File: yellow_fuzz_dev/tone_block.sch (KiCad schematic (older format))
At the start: 34 parts

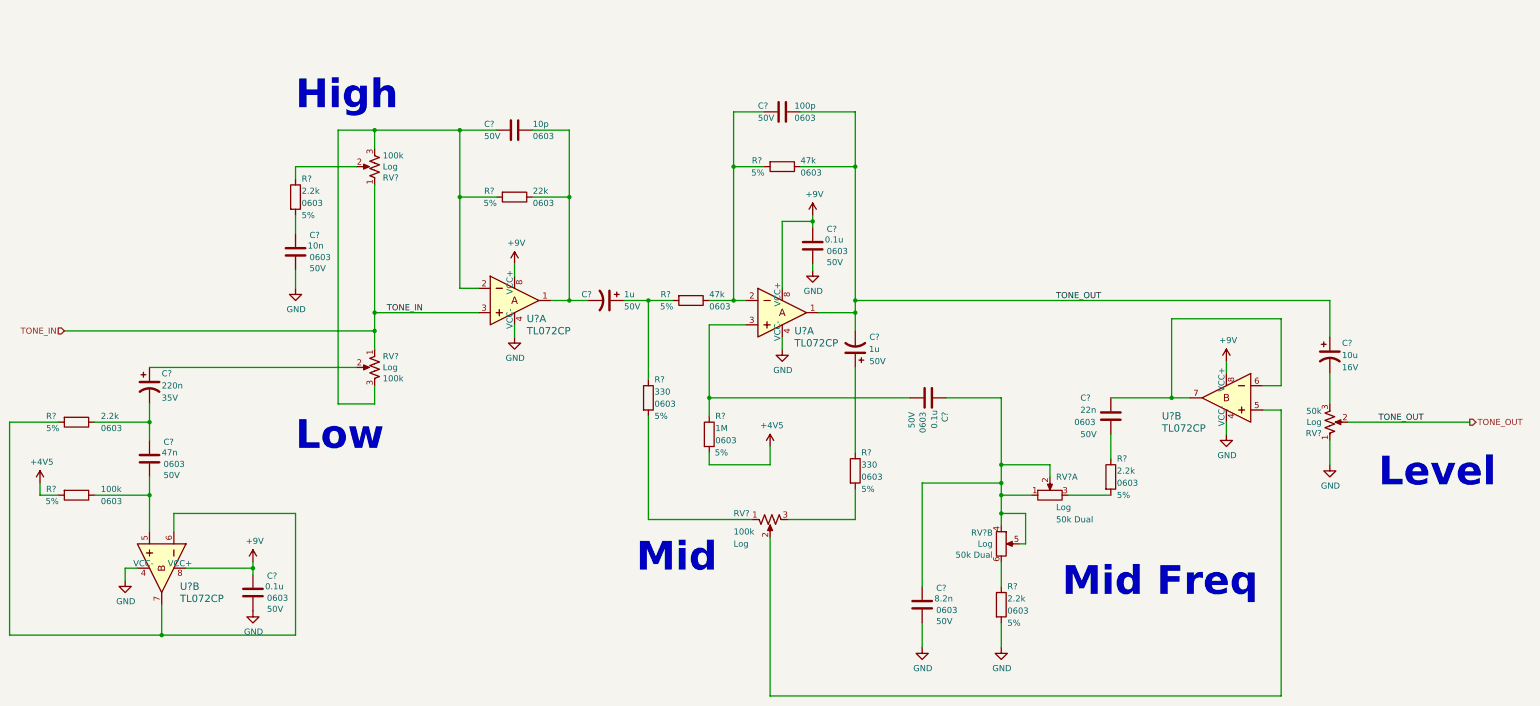
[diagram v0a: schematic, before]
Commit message: moved footprints into PCB
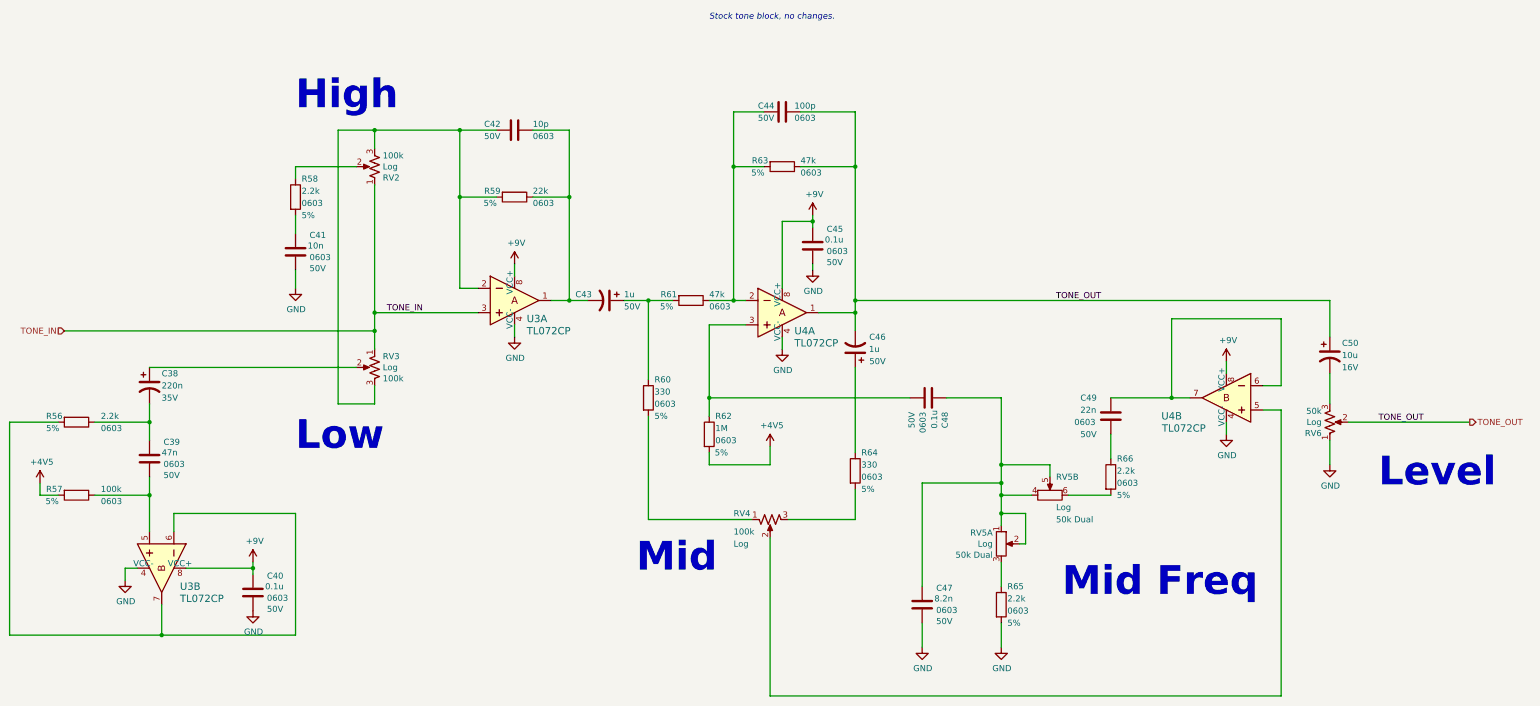
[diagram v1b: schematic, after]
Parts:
- C38, C50: renamed from C?; footprint (none) -> Capacitor_THT:CP_Radial_D5.0mm_P2.00mm
- C43, C46: renamed from C?; footprint (none) -> Capacitor_THT:CP_Radial_D4.0mm_P1.50mm
- U3, U4: renamed from U?; footprint digikey-footprints:DIP-8_W7.62mm -> digikey:DIP-8_W7.62mm
- gave numbers to parts that had none: 25
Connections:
- net at R65.1: now also RV5.3; no longer RV5.6
- net at R66.2: now also RV5.6; no longer RV5.3
- new net: C47.1, C48.1, RV5.1, RV5.2, RV5.4, RV5.5
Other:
- note added: "Stock tone block, no changes."

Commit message: added 3d to connector and DIP footprints, moved to project lib, updated PCB
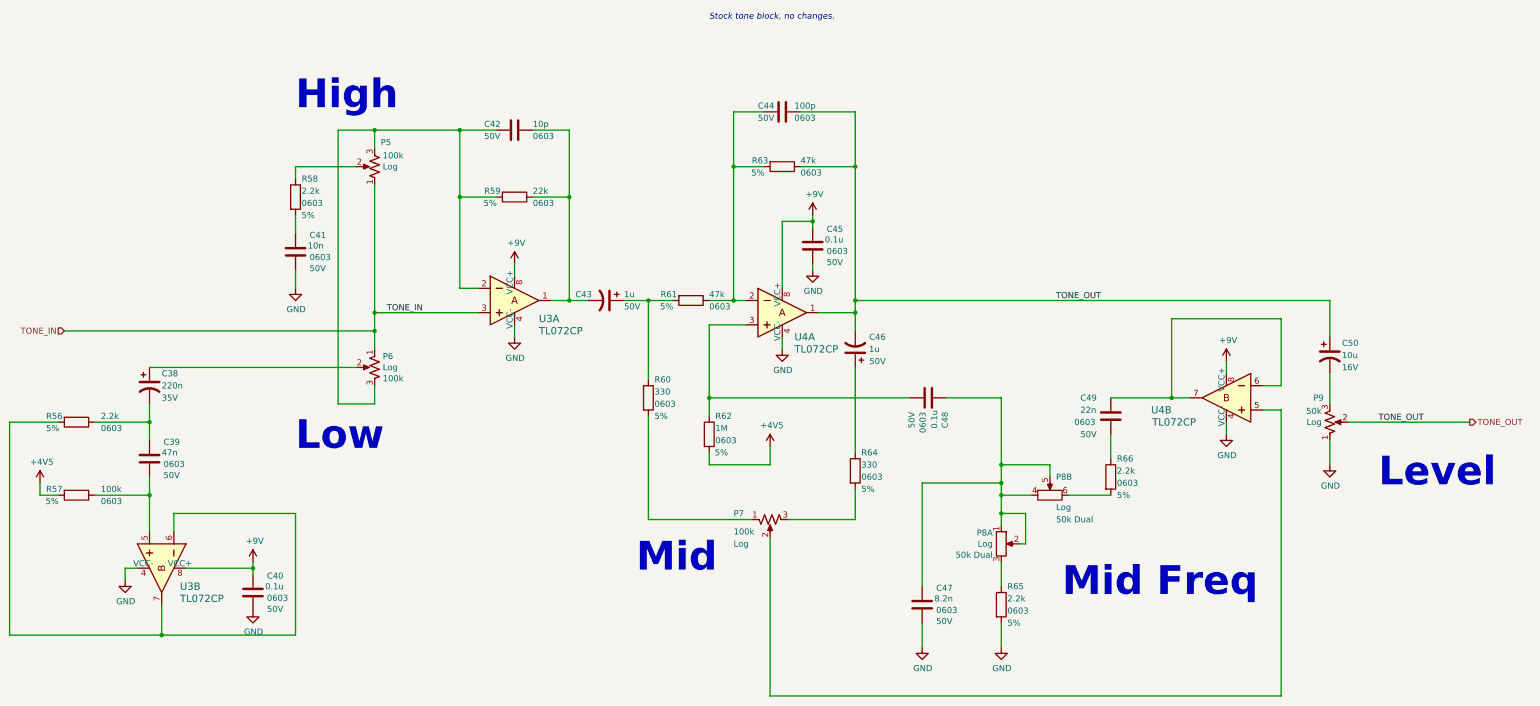
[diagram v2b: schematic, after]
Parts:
- removed U3, U4: TL072CP, digikey:DIP-8_W7.62mm, symbol dk_opamps:TL072CP
- added U3, U4: TL072CP, yellow_fuzz_dev:DIP-8_W7.62mm, symbol yellow_fuzz_dev:TL072CP
- renumbered RV2 to P5, RV3 to P6, RV4 to P7, RV5 to P8, RV6 to P9
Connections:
- net +9V: now also U3.8 (VCC+), U3.8 (VCC+), U4.8 (VCC+), U4.8 (VCC+)
- net GND: now also U3.4 (VCC-), U3.4 (VCC-), U4.4 (VCC-), U4.4 (VCC-)
- net TONE_IN: now also U3.3
- net TONE_OUT: now also U4.1
- net at C42.1, C43.2, R59.1: now also U3.1
- net at C42.2, P5.3, P6.3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: now also U3.2
- net at C44.2, R61.1, R63.2: now also U4.2
- net at R56.2: now also U3.6, U3.7
- net at C39.2, R57.1: now also U3.5
- net at C48.2, R62.1: now also U4.3
- net at P7.2: now also U4.5
- net at C49.1: now also U4.6, U4.7

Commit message: updated potentiometers to use the same mechanical family throughout
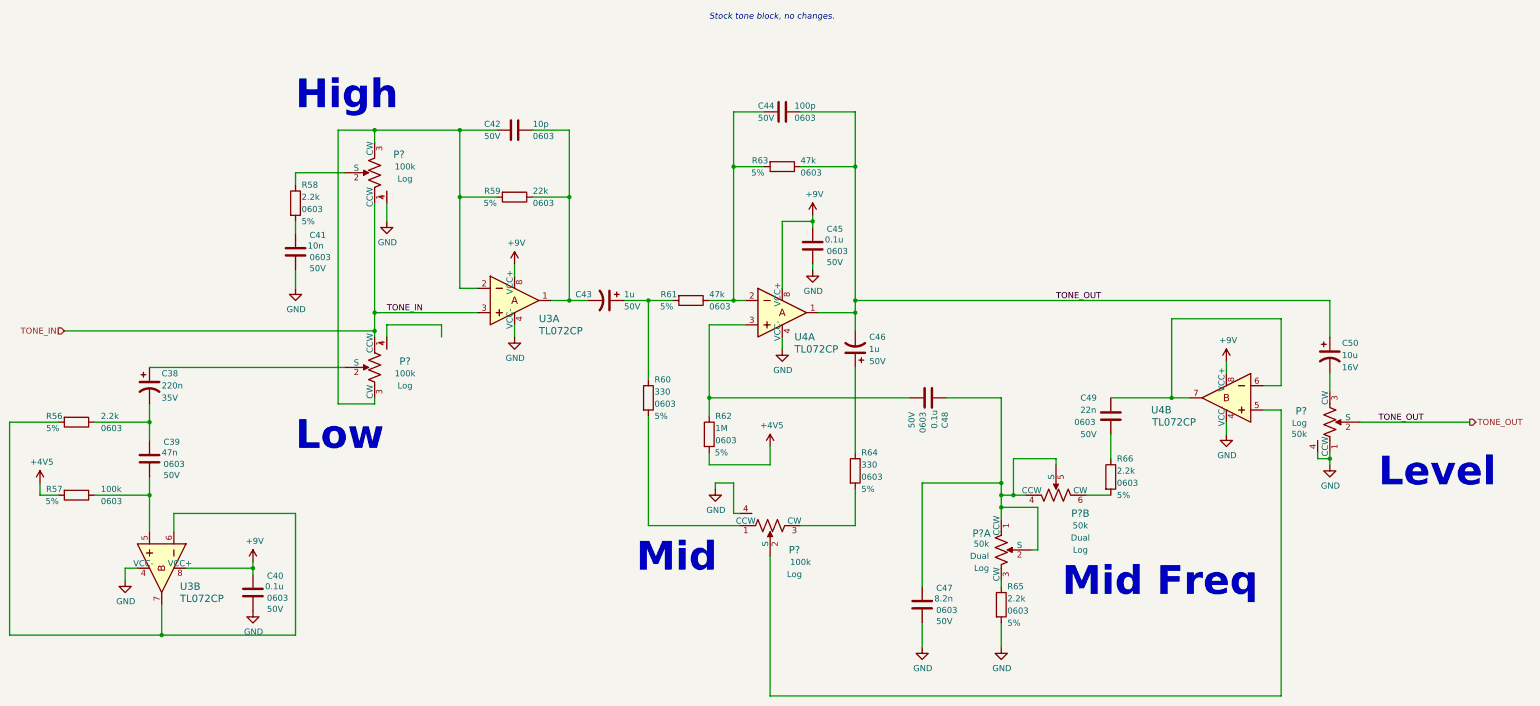
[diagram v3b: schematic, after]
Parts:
- removed P5, P6, P7: R_POT_US, yellow_fuzz_dev:Potentiometer_Bourns_PTV111_4420A_Single_Vertical, symbol Device:R_POT_US
- removed P8: R_POT_Dual_Separate, yellow_fuzz_dev:Potentiometer_Bourns_PTV112_3417A_Dual_Vertical, symbol Device:R_POT_Dual_Separate
- removed P9: R_POT_US, yellow_fuzz_dev:Potentiometer_Bourns_PCW1J_R24_B_Single_Vertical, symbol Device:R_POT_US
- added P? (x2): PTV112-4420A-A503, yellow_fuzz_dev:Potentiometer_Bourns_PTV112_3417A_Dual_Vertical, symbol yellow_fuzz_dev:PTV112-4420A-A503
- added P?: PTV111-4420A-A503, yellow_fuzz_dev:Potentiometer_Bourns_PTV111_4420A_Single_Vertical, symbol yellow_fuzz_dev:PTV111-4420A-A503
- added P? (x3): PTV111-4420A-A104, yellow_fuzz_dev:Potentiometer_Bourns_PTV111_4420A_Single_Vertical, symbol yellow_fuzz_dev:PTV111-4420A-A104
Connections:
- net GND: now also P?.1 (CCW), P?.4, P?.4, P?.4
- net TONE_IN: now also P?.1 (CCW), P?.1 (CCW)
- net TONE_OUT: now also P?.2 (S)
- net at C50.2: now also P?.3 (CW)
- net at C47.1, C48.1: now also P?.1 (CCW), P?.2 (S), P?.4 (CCW), P?.5 (S)
- net at R65.1: now also P?.3 (CW)
- net at C42.2, R59.2, U3.2: now also P?.3 (CW), P?.3 (CW)
- net at R60.2: now also P?.1 (CCW)
- net at R58.1: now also P?.2 (S)
- net at C38.1: now also P?.2 (S)
- net at R64.2: now also P?.3 (CW)
- net at U4.5: now also P?.2 (S)
- net at R66.2: now also P?.6 (CW)
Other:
- moved on the sheet: R58

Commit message: first draft placement done. Added ampharos logo.
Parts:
- gave numbers to parts that had none: 5
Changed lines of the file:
@@
-$EndComp
-$Comp
-L Device:CP1 C46
-U 1 1 5EA96593
-P 9050 4850
-F 0 "C46" H 8800 4750 50  0000 L CNN
-F 1 "1u" H 8850 4850 50  0000 L CNN
-F 2 "Capacitor_THT:CP_Radial_D4.0mm_P1.50mm" H 9050 4850 50  0001 C CNN
-F 3 "~" H 9050 4850 50  0001 C CNN
-F 4 "Nichicon" H 9050 4850 50  0001 C CNN "Manufacturer"
-F 5 "UST1H010MDD1TE" H 9050 4850 50  0001 C CNN "Manufacturer PN"
-F 6 "Digi-Key" H 9050 4850 50  0001 C CNN "Supplier"
-F 7 "493-17436-1-ND" H 9050 4850 50  0001 C CNN "Supplier PN"
-F 8 "50V" H 8800 4950 50  0000 L CNN "Voltage"
-	1    9050 4850
-	-1   0    0    1
-$EndComp
-$Comp
-L Device:R R60
-U 1 1 5EA965A0
-P 7350 5250
-F 0 "R60" H 7400 5400 50  0000 L CNN
-F 1 "330" H 7400 5300 50  0000 L CNN
-F 2 "Resistor_SMD:R_0603_1608Metric_Pad1.05x0.95mm_HandSolder" V 7280 5250 50  0001 C CNN
-F 3 "~" H 7350 5250 50  0001 C CNN
-F 4 "CR0603-JW-331ELF" H 7350 5250 50  0001 C CNN "Manufacturer PN"
-F 5 "5%" H 7400 5100 50  0000 L CNN "Tolerance"
-F 6 "Bourns Inc." H 7350 5250 50  0001 C CNN "Manufacturer"
-F 7 "Digi-Key" H 7350 5250 50  0001 C CNN "Supplier"
-F 8 "CR0603-JW-331ELFCT-ND" H 7350 5250 50  0001 C CNN "Supplier PN"
-F 9 "0.1 W" H 7350 5250 50  0001 C CNN "Power"
-F 10 "0603" H 7400 5200 50  0000 L CNN "Package"
-	1    7350 5250
-	1    0    0    -1
 $EndComp
 $Comp
@@
 $EndComp
 $Comp
-L Device:R R64
-U 1 1 5EA96609
-P 9050 5850
-F 0 "R64" H 9100 6000 50  0000 L CNN
-F 1 "330" H 9100 5900 50  0000 L CNN
-F 2 "Resistor_SMD:R_0603_1608Metric_Pad1.05x0.95mm_HandSolder" V 8980 5850 50  0001 C CNN
-F 3 "~" H 9050 5850 50  0001 C CNN
-F 4 "CR0603-JW-331ELF" H 9050 5850 50  0001 C CNN "Manufacturer PN"
-F 5 "5%" H 9100 5700 50  0000 L CNN "Tolerance"
-F 6 "Bourns Inc." H 9050 5850 50  0001 C CNN "Manufacturer"
-F 7 "Digi-Key" H 9050 5850 50  0001 C CNN "Supplier"
-F 8 "CR0603-JW-331ELFCT-ND" H 9050 5850 50  0001 C CNN "Supplier PN"
-F 9 "0.1 W" H 9050 5850 50  0001 C CNN "Power"
-F 10 "0603" H 9100 5800 50  0000 L CNN "Package"
-	1    9050 5850
-	1    0    0    -1
-$EndComp
-$Comp
 L Device:R R62
 U 1 1 5EA96616
@@
 $EndComp
 $Comp
-L Device:C C48
-U 1 1 5EA96628
-P 9650 5250
-F 0 "C48" H 9765 5387 50  0000 L CNN
-F 1 "0.1u" H 9750 5300 50  0000 L CNN
-F 2 "Capacitor_SMD:C_0603_1608Metric_Pad1.05x0.95mm_HandSolder" H 9688 5100 50  0001 C CNN
-F 3 "~" H 9650 5250 50  0001 C CNN
-F 4 "KEMET" H 9650 5250 50  0001 C CNN "Manufacturer"
-F 5 "C0603C104M5RACTU" H 9650 5250 50  0001 C CNN "Manufacturer PN"
-F 6 "Digi-Key" H 9650 5250 50  0001 C CNN "Supplier"
-F 7 "399-7845-1-ND" H 9650 5250 50  0001 C CNN "Supplier PN"
-F 8 "0603" H 9765 5205 50  0000 L CNN "Package"
-F 9 "50V" H 9765 5114 50  0000 L CNN "Voltage"
-	1    9650 5250
-	0    1    1    0
-$EndComp
-$Comp
 L Device:C C47
 U 1 1 5EA96664
@@
 	8150 4450 8050 4450
 Wire Wire Line
-	7550 4450 7350 4450
-Wire Wire Line
 	6850 4450 6700 4450
 Connection ~ 6700 4450
 Wire Wire Line
-	7350 5100 7350 4450
-Connection ~ 7350 4450
-Wire Wire Line
-	7350 4450 7150 4450
-Wire Wire Line
-	7850 5400 7850 5250
-Wire Wire Line
 	7850 4650 8150 4650
 Wire Wire Line
-	9050 5700 9050 5000
-Wire Wire Line
 	9050 4700 9050 4550
 Wire Wire Line
@@
 Wire Wire Line
 	7850 5800 7850 5700
-Wire Wire Line
-	9500 5250 7850 5250
-Connection ~ 7850 5250
-Wire Wire Line
-	7850 5250 7850 4650
 Wire Wire Line
 	8300 3350 8050 3350
@@
 	10350 6050 10250 6050
 $Comp
-L yellow_fuzz_dev:PTV112-4420A-A503 P?
+L yellow_fuzz_dev:PTV112-4420A-A503 P8
 U 1 1 5EB07C1A
 P 10250 6750
-F 0 "P?" V 9864 6663 60  0000 R CNN
+F 0 "P8" V 9864 6663 60  0000 R CNN
 F 1 "PTV112-4420A-A503" H 10440 6770 60  0001 L CNN
 F 2 "yellow_fuzz_dev:Potentiometer_Bourns_PTV112_3417A_Dual_Vertical" H 10450 6950 60  0001 L CNN
@@
 $EndComp
 $Comp
-L yellow_fuzz_dev:PTV112-4420A-A503 P?
+L yellow_fuzz_dev:PTV112-4420A-A503 P8
 U 2 1 5EB096B3
 P 10950 6050
-F 0 "P?" H 10900 5900 60  0000 C CNN
+F 0 "P8" H 10900 5900 60  0000 C CNN
 F 1 "PTV112-4420A-A503" H 11140 6070 60  0001 L CNN
 F 2 "yellow_fuzz_dev:Potentiometer_Bourns_PTV112_3417A_Dual_Vertical" H 11150 6250 60  0001 L CNN
@@
 $EndComp
 $Comp
-L yellow_fuzz_dev:PTV111-4420A-A503 P?
+L yellow_fuzz_dev:PTV111-4420A-A503 P9
 U 1 1 5EB0A21B
 P 12950 5200
-F 0 "P?" V 12791 5012 60  0000 R CNN
+F 0 "P9" V 12791 5012 60  0000 R CNN
 F 1 "PTV111-4420A-A503" H 13140 5220 60  0001 L CNN
 F 2 "yellow_fuzz_dev:Potentiometer_Bourns_PTV111_4420A_Single_Vertical" H 13150 5400 60  0001 L CNN
@@
 	12950 5050 12950 5200
 $Comp
-L yellow_fuzz_dev:PTV111-4420A-A104 P?
+L yellow_fuzz_dev:PTV111-4420A-A104 P7
 U 1 1 5EB2E1DB
 P 8600 6300
-F 0 "P?" H 8550 6500 60  0000 C CNN
+F 0 "P7" H 8550 6500 60  0000 C CNN
 F 1 "PTV111-4420A-A104" H 8790 6320 60  0001 L CNN
 F 2 "yellow_fuzz_dev:Potentiometer_Bourns_PTV111_4420A_Single_Vertical" H 8800 6500 60  0001 L CNN
@@
 $EndComp
 $Comp
-L power:GND #PWR?
+L power:GND #PWR06
 U 1 1 5EB37E5F
 P 7900 6000
-F 0 "#PWR?" H 7900 5750 50  0001 C CNN
+F 0 "#PWR06" H 7900 5750 50  0001 C CNN
 F 1 "GND" H 7905 5827 50  0000 C CNN
 F 2 "" H 7900 6000 50  0001 C CNN
@@
 	8600 6300 9050 6300
 Wire Wire Line
-	9050 6000 9050 6300
-Wire Wire Line
 	8350 6550 8350 7700
 $Comp
-L yellow_fuzz_dev:PTV111-4420A-A104 P?
+L yellow_fuzz_dev:PTV111-4420A-A104 P5
 U 1 1 5EB4825A
 P 5100 3150
-F 0 "P?" V 5000 2950 60  0000 C CNN
+F 0 "P5" V 5000 2950 60  0000 C CNN
 F 1 "PTV111-4420A-A104" H 5290 3170 60  0001 L CNN
 F 2 "yellow_fuzz_dev:Potentiometer_Bourns_PTV111_4420A_Single_Vertical" H 5300 3350 60  0001 L CNN
@@
 $EndComp
 $Comp
-L yellow_fuzz_dev:PTV111-4420A-A104 P?
+L yellow_fuzz_dev:PTV111-4420A-A104 P6
 U 1 1 5EB49413
 P 5100 5250
-F 0 "P?" V 4800 5000 60  0000 C CNN
+F 0 "P6" V 4800 5000 60  0000 C CNN
 F 1 "PTV111-4420A-A104" H 5290 5270 60  0001 L CNN
 F 2 "yellow_fuzz_dev:Potentiometer_Bourns_PTV111_4420A_Single_Vertical" H 5300 5450 60  0001 L CNN
@@
 Connection ~ 5100 4550
 $Comp
-L power:GND #PWR?
+L power:GND #PWR05
 U 1 1 5EB779C0
 P 5200 3800
-F 0 "#PWR?" H 5200 3550 50  0001 C CNN
+F 0 "#PWR05" H 5200 3550 50  0001 C CNN
 F 1 "GND" H 5205 3627 50  0000 C CNN
 F 2 "" H 5200 3800 50  0001 C CNN
@@
 Wire Wire Line
 	5200 3650 5200 3800
+Wire Wire Line
+	9050 6000 9050 6300
+$Comp
+L Device:R R64
+U 1 1 5EA96609
+P 9050 5850
+F 0 "R64" H 9100 6000 50  0000 L CNN
+F 1 "330" H 9100 5900 50  0000 L CNN
+F 2 "Resistor_SMD:R_0603_1608Metric_Pad1.05x0.95mm_HandSolder" V 8980 5850 50  0001 C CNN
+F 3 "~" H 9050 5850 50  0001 C CNN
+F 4 "CR0603-JW-331ELF" H 9050 5850 50  0001 C CNN "Manufacturer PN"
+F 5 "5%" H 9100 5700 50  0000 L CNN "Tolerance"
+F 6 "Bourns Inc." H 9050 5850 50  0001 C CNN "Manufacturer"
+F 7 "Digi-Key" H 9050 5850 50  0001 C CNN "Supplier"
+F 8 "CR0603-JW-331ELFCT-ND" H 9050 5850 50  0001 C CNN "Supplier PN"
+F 9 "0.1 W" H 9050 5850 50  0001 C CNN "Power"
+F 10 "0603" H 9100 5800 50  0000 L CNN "Package"
+	1    9050 5850
+	1    0    0    -1
+$EndComp
+Connection ~ 7350 4450
+Wire Wire Line
+	7350 4450 7150 4450
+Wire Wire Line
+	7550 4450 7350 4450
+Wire Wire Line
+	9050 5700 9050 5000
+Wire Wire Line
+	7850 5250 7850 4650
+Connection ~ 7850 5250
+Wire Wire Line
+	9500 5250 7850 5250
+Wire Wire Line
+	7850 5400 7850 5250
+Wire Wire Line
+	7350 5100 7350 4450
+$Comp
+L Device:C C48
+U 1 1 5EA96628
+P 9650 5250
+F 0 "C48" H 9765 5387 50  0000 L CNN
+F 1 "0.1u" H 9750 5300 50  0000 L CNN
+F 2 "Capacitor_SMD:C_0603_1608Metric_Pad1.05x0.95mm_HandSolder" H 9688 5100 50  0001 C CNN
+F 3 "~" H 9650 5250 50  0001 C CNN
+F 4 "KEMET" H 9650 5250 50  0001 C CNN "Manufacturer"
+F 5 "C0603C104M5RACTU" H 9650 5250 50  0001 C CNN "Manufacturer PN"
+F 6 "Digi-Key" H 9650 5250 50  0001 C CNN "Supplier"
+F 7 "399-7845-1-ND" H 9650 5250 50  0001 C CNN "Supplier PN"
+F 8 "0603" H 9765 5205 50  0000 L CNN "Package"
+F 9 "50V" H 9765 5114 50  0000 L CNN "Voltage"
+	1    9650 5250
+	0    1    1    0
+$EndComp
+$Comp
+L Device:R R60
+U 1 1 5EA965A0
+P 7350 5250
+F 0 "R60" H 7400 5400 50  0000 L CNN
+F 1 "330" H 7400 5300 50  0000 L CNN
+F 2 "Resistor_SMD:R_0603_1608Metric_Pad1.05x0.95mm_HandSolder" V 7280 5250 50  0001 C CNN
+F 3 "~" H 7350 5250 50  0001 C CNN
+F 4 "CR0603-JW-331ELF" H 7350 5250 50  0001 C CNN "Manufacturer PN"
+F 5 "5%" H 7400 5100 50  0000 L CNN "Tolerance"
+F 6 "Bourns Inc." H 7350 5250 50  0001 C CNN "Manufacturer"
+F 7 "Digi-Key" H 7350 5250 50  0001 C CNN "Supplier"
+F 8 "CR0603-JW-331ELFCT-ND" H 7350 5250 50  0001 C CNN "Supplier PN"
+F 9 "0.1 W" H 7350 5250 50  0001 C CNN "Power"
+F 10 "0603" H 7400 5200 50  0000 L CNN "Package"
+	1    7350 5250
+	1    0    0    -1
+$EndComp
+$Comp
+L Device:CP1 C46
+U 1 1 5EA96593
+P 9050 4850
+F 0 "C46" H 8800 4750 50  0000 L CNN
+F 1 "1u" H 8850 4850 50  0000 L CNN
+F 2 "Capacitor_THT:CP_Radial_D4.0mm_P1.50mm" H 9050 4850 50  0001 C CNN
+F 3 "~" H 9050 4850 50  0001 C CNN
+F 4 "Nichicon" H 9050 4850 50  0001 C CNN "Manufacturer"
+F 5 "UST1H010MDD1TE" H 9050 4850 50  0001 C CNN "Manufacturer PN"
+F 6 "Digi-Key" H 9050 4850 50  0001 C CNN "Supplier"
+F 7 "493-17436-1-ND" H 9050 4850 50  0001 C CNN "Supplier PN"
+F 8 "50V" H 8800 4950 50  0000 L CNN "Voltage"
+	1    9050 4850
+	-1   0    0    1
+$EndComp
 $EndSCHEMATC
